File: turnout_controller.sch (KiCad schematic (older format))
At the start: 29 parts, among them J1 DCC_A, J2 DCC_B, J3 PROG, J4 MOT_CNTL, J5 MOT_POWER, J6 MOT_GND, J7 LED_1, J8 LED_2, SW1 SW_Push, SW2 SW_Push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

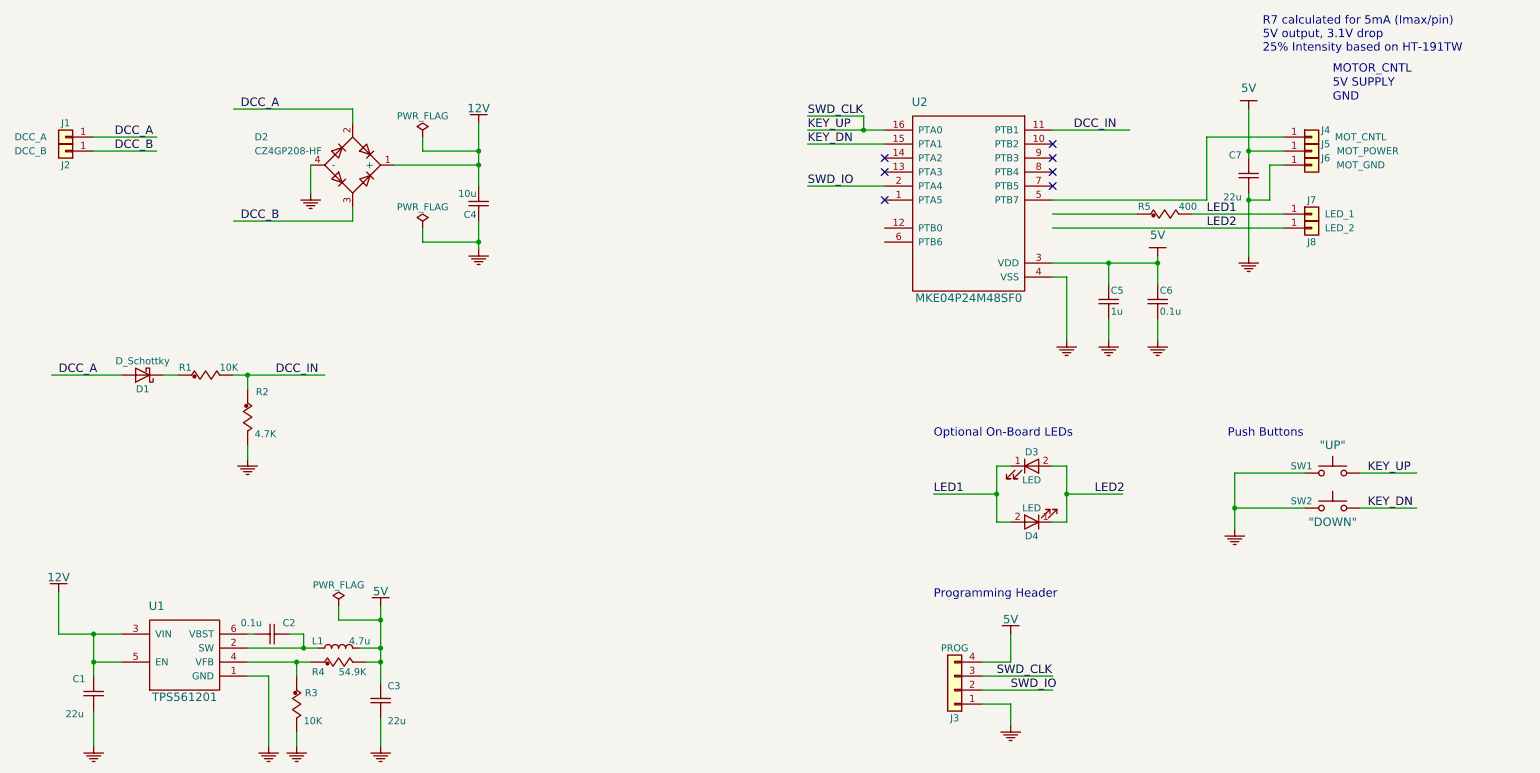
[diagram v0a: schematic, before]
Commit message: Board revision 3.0 - prog header @ top
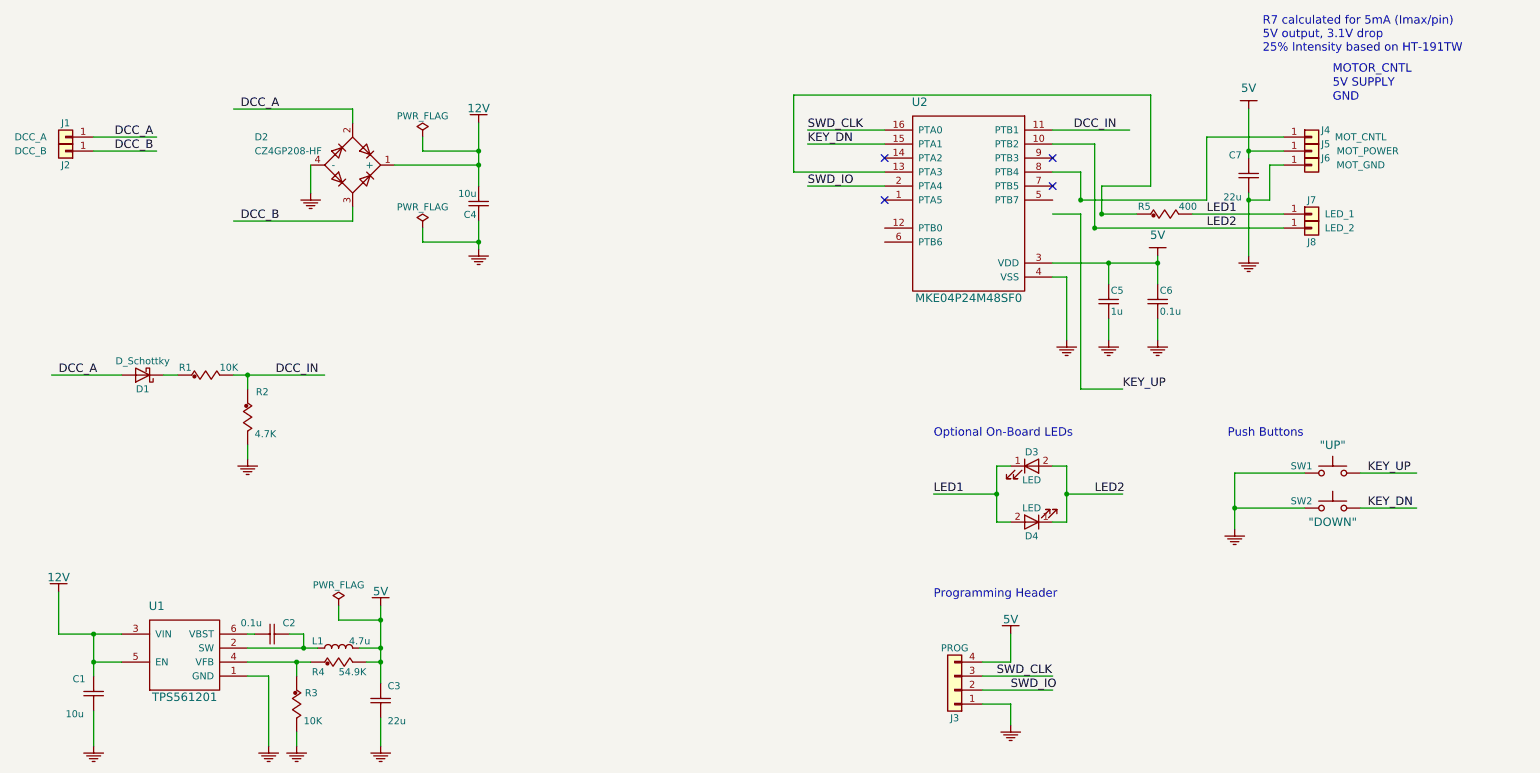
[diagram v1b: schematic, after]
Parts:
- C1: value 22u -> 10u
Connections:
- wire segments 83 -> 94
- no-connect marks 7 -> 4
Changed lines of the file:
@@
 $EndComp
 NoConn ~ 7950 1600
-NoConn ~ 7950 1700
 NoConn ~ 7950 1800
 NoConn ~ 6750 1600
-NoConn ~ 6750 1700
-Text Label 6200 1400 0    60   ~ 0
+Text Label 8450 3250 0    60   ~ 0
 KEY_UP
 Text Label 6200 1500 0    60   ~ 0
@@
 Text Label 2400 3150 0    60   ~ 0
 DCC_IN
-NoConn ~ 7950 1500
 Text Notes 9450 850  0    60   ~ 0
 R7 calculated for 5mA (Imax/pin)\n5V output, 3.1V drop\n25% Intensity based on HT-191TW\n
@@
 	1    0    0    -1
 $EndComp
-Text Label 6200 1300 0    60   ~ 0
+Text Label 6200 1400 0    60   ~ 0
 SWD_CLK
 NoConn ~ 6750 1900
@@
 	0    -1   -1   0
 $EndComp
-Wire Wire Line
-	7950 2450 8050 2450
-Wire Wire Line
-	7950 2350 8700 2350
-Connection ~ 8350 2350
-Wire Wire Line
-	7950 2000 8550 2000
-Wire Wire Line
-	7950 1900 9050 1900
-Wire Wire Line
-	8950 2000 9600 2000
-Wire Wire Line
-	3850 1350 3850 1800
-Connection ~ 3850 1650
-Wire Wire Line
-	3850 2050 3850 2250
-Wire Wire Line
-	8350 2350 8350 2500
-Wire Wire Line
-	8700 2300 8700 2500
-Wire Wire Line
-	2200 3650 2200 3750
-Wire Wire Line
-	2650 1650 2650 1850
-Wire Wire Line
-	2950 1950 2950 2050
-Wire Wire Line
-	2950 2050 2100 2050
-Wire Wire Line
-	1100 1550 1550 1550
-Wire Wire Line
-	1100 1450 1550 1450
-Wire Wire Line
-	2100 1250 2950 1250
-Wire Wire Line
-	7950 1400 8500 1400
-Wire Wire Line
-	1600 3150 1700 3150
-Wire Wire Line
-	2100 3150 2750 3150
-Wire Wire Line
-	2200 3150 2200 3250
-Connection ~ 2200 3150
-Wire Wire Line
-	8050 2450 8050 2900
-Wire Wire Line
-	8350 2750 8350 2900
-Wire Wire Line
-	8700 2750 8700 2900
-Wire Wire Line
-	9350 1850 9350 2300
-Wire Wire Line
-	9500 1650 9600 1650
-Wire Wire Line
-	9050 1900 9050 1450
-Wire Wire Line
-	9050 1450 9600 1450
-Wire Wire Line
-	9350 1900 9500 1900
-Wire Wire Line
-	9500 1900 9500 1650
-Connection ~ 9350 1900
-Wire Wire Line
-	6200 1500 6750 1500
-Wire Wire Line
-	3250 1650 3850 1650
-Connection ~ 8700 2350
-Wire Wire Line
-	6200 1400 6750 1400
-Wire Wire Line
-	10150 4100 10550 4100
-Wire Wire Line
-	10550 3850 10150 3850
-Wire Wire Line
-	9250 3850 9750 3850
-Wire Wire Line
-	9250 3850 9250 4250
-Wire Wire Line
-	9250 4100 9750 4100
-Connection ~ 9250 4100
-Wire Wire Line
-	2950 1250 2950 1350
-Wire Wire Line
-	1300 3150 800  3150
-Wire Wire Line
-	3450 1450 3450 1550
-Wire Wire Line
-	3450 1550 3850 1550
-Connection ~ 3850 1550
-Wire Wire Line
-	3450 2100 3450 2200
-Wire Wire Line
-	3450 2200 3850 2200
-Connection ~ 3850 2200
-Wire Wire Line
-	9350 1250 9350 1600
-Wire Wire Line
-	9600 1550 9350 1550
-Connection ~ 9350 1550
-Wire Wire Line
-	6600 1300 6600 1400
-Wire Wire Line
-	6200 1300 6600 1300
-Connection ~ 6600 1400
-Wire Wire Line
-	6750 1800 6200 1800
-Wire Wire Line
-	7450 5300 7950 5300
-Wire Wire Line
-	7450 5400 7950 5400
-Wire Wire Line
-	7450 5200 7650 5200
-Wire Wire Line
-	7650 5200 7650 5000
-Wire Wire Line
-	7450 5500 7650 5500
-Wire Wire Line
-	7650 5500 7650 5650
-Wire Wire Line
-	7550 4200 7650 4200
-Wire Wire Line
-	7550 3800 7550 4200
-Wire Wire Line
-	7550 3800 7650 3800
-Wire Wire Line
-	8050 4200 7950 4200
-Wire Wire Line
-	8050 3800 8050 4200
-Wire Wire Line
-	8050 3800 7950 3800
-Connection ~ 7550 4000
-Connection ~ 8050 4000
-Wire Wire Line
-	7950 2100 9600 2100
-Wire Wire Line
-	7100 4000 7550 4000
-Wire Wire Line
-	8050 4000 8450 4000
-Wire Wire Line
-	2200 5300 2350 5300
-Wire Wire Line
-	2350 5300 2350 5800
-Wire Wire Line
-	850  5000 1300 5000
-Wire Wire Line
-	850  5000 850  4700
-Wire Wire Line
-	1100 5000 1100 5300
-Connection ~ 1100 5000
 $Comp
 L CAP_NP C1
@@
 P 1100 5550
 F 0 "C1" H 950 5750 50  0000 L BNN
-F 1 "22u" H 900 5500 50  0000 L BNN
+F 1 "10u" H 900 5500 50  0000 L BNN
 F 2 "Capacitors_SMD:C_0603_HandSoldering" H 1175 5450 40  0001 L BNN
 F 3 "" H 1100 5550 60  0000 C CNN
@@
 	1    0    0    -1
 $EndComp
-Wire Wire Line
-	1100 5550 1100 5800
-Wire Wire Line
-	1300 5200 1100 5200
-Connection ~ 1100 5200
-Wire Wire Line
-	2200 5100 2700 5100
-Wire Wire Line
-	2200 5200 2650 5200
-Wire Wire Line
-	2550 5200 2550 5300
-Wire Wire Line
-	2550 5700 2550 5800
-Connection ~ 2550 5200
 $Comp
 L CAP_NP C3
@@
 	1    0    0    -1
 $EndComp
-Wire Wire Line
-	3150 5200 3050 5200
-Wire Wire Line
-	3150 4800 3150 5350
-Wire Wire Line
-	3000 5100 3150 5100
-Connection ~ 3150 5200
-Connection ~ 3150 5100
-Wire Wire Line
-	2850 4800 2850 4900
-Wire Wire Line
-	2850 4900 3150 4900
-Connection ~ 3150 4900
 $Comp
 L GND_ #PWR022
@@
 	1    0    0    -1
 $EndComp
-Wire Wire Line
-	3150 5800 3150 5600
 $Comp
 L CAP_NP C2
@@
 $EndComp
 Wire Wire Line
+	7950 2450 8050 2450
+Wire Wire Line
+	7950 2350 8700 2350
+Connection ~ 8350 2350
+Wire Wire Line
+	8300 2000 8550 2000
+Wire Wire Line
+	8150 1900 9050 1900
+Wire Wire Line
+	8950 2000 9600 2000
+Wire Wire Line
+	3850 1350 3850 1800
+Connection ~ 3850 1650
+Wire Wire Line
+	3850 2050 3850 2250
+Wire Wire Line
+	8350 2350 8350 2500
+Wire Wire Line
+	8700 2300 8700 2500
+Wire Wire Line
+	2200 3650 2200 3750
+Wire Wire Line
+	2650 1650 2650 1850
+Wire Wire Line
+	2950 1950 2950 2050
+Wire Wire Line
+	2950 2050 2100 2050
+Wire Wire Line
+	1100 1550 1550 1550
+Wire Wire Line
+	1100 1450 1550 1450
+Wire Wire Line
+	2100 1250 2950 1250
+Wire Wire Line
+	7950 1400 8500 1400
+Wire Wire Line
+	1600 3150 1700 3150
+Wire Wire Line
+	2100 3150 2750 3150
+Wire Wire Line
+	2200 3150 2200 3250
+Connection ~ 2200 3150
+Wire Wire Line
+	8050 2450 8050 2900
+Wire Wire Line
+	8350 2750 8350 2900
+Wire Wire Line
+	8700 2750 8700 2900
+Wire Wire Line
+	9350 1850 9350 2300
+Wire Wire Line
+	9500 1650 9600 1650
+Wire Wire Line
+	9050 1900 9050 1450
+Wire Wire Line
+	9050 1450 9600 1450
+Wire Wire Line
+	9350 1900 9500 1900
+Wire Wire Line
+	9500 1900 9500 1650
+Connection ~ 9350 1900
+Wire Wire Line
+	6200 1500 6750 1500
+Wire Wire Line
+	3250 1650 3850 1650
+Connection ~ 8700 2350
+Wire Wire Line
+	10150 4100 10550 4100
+Wire Wire Line
+	10550 3850 10150 3850
+Wire Wire Line
+	9250 3850 9750 3850
+Wire Wire Line
+	9250 3850 9250 4250
+Wire Wire Line
+	9250 4100 9750 4100
+Connection ~ 9250 4100
+Wire Wire Line
+	2950 1250 2950 1350
+Wire Wire Line
+	1300 3150 800  3150
+Wire Wire Line
+	3450 1450 3450 1550
+Wire Wire Line
+	3450 1550 3850 1550
+Connection ~ 3850 1550
+Wire Wire Line
+	3450 2100 3450 2200
+Wire Wire Line
+	3450 2200 3850 2200
+Connection ~ 3850 2200
+Wire Wire Line
+	9350 1250 9350 1600
+Wire Wire Line
+	9600 1550 9350 1550
+Connection ~ 9350 1550
+Wire Wire Line
+	6750 1800 6200 1800
+Wire Wire Line
+	7450 5300 7950 5300
+Wire Wire Line
+	7450 5400 7950 5400
+Wire Wire Line
+	7450 5200 7650 5200
+Wire Wire Line
+	7650 5200 7650 5000
+Wire Wire Line
+	7450 5500 7650 5500
+Wire Wire Line
+	7650 5500 7650 5650
+Wire Wire Line
+	7550 4200 7650 4200
+Wire Wire Line
+	7550 3800 7550 4200
+Wire Wire Line
+	7550 3800 7650 3800
+Wire Wire Line
+	8050 4200 7950 4200
+Wire Wire Line
+	8050 3800 8050 4200
+Wire Wire Line
+	8050 3800 7950 3800
+Connection ~ 7550 4000
+Connection ~ 8050 4000
+Wire Wire Line
+	8250 2100 9600 2100
+Wire Wire Line
+	7100 4000 7550 4000
+Wire Wire Line
+	8050 4000 8450 4000
+Wire Wire Line
+	2200 5300 2350 5300
+Wire Wire Line
+	2350 5300 2350 5800
+Wire Wire Line
+	850  5000 1300 5000
+Wire Wire Line
+	850  5000 850  4700
+Wire Wire Line
+	1100 5000 1100 5300
+Connection ~ 1100 5000
+Wire Wire Line
+	1100 5550 1100 5800
+Wire Wire Line
+	1300 5200 1100 5200
+Connection ~ 1100 5200
+Wire Wire Line
+	2200 5100 2700 5100
+Wire Wire Line
+	2200 5200 2650 5200
+Wire Wire Line
+	2550 5200 2550 5300
+Wire Wire Line
+	2550 5700 2550 5800
+Connection ~ 2550 5200
+Wire Wire Line
+	3150 5200 3050 5200
+Wire Wire Line
+	3150 4800 3150 5350
+Wire Wire Line
+	3000 5100 3150 5100
+Connection ~ 3150 5200
+Connection ~ 3150 5100
+Wire Wire Line
+	2850 4800 2850 4900
+Wire Wire Line
+	2850 4900 3150 4900
+Connection ~ 3150 4900
+Wire Wire Line
+	3150 5800 3150 5600
+Wire Wire Line
 	2500 5000 2600 5000
 Wire Wire Line
@@
 Wire Wire Line
 	2250 5000 2200 5000
+Wire Wire Line
+	6750 1700 6100 1700
+Wire Wire Line
+	6100 1700 6100 1150
+Wire Wire Line
+	6100 1150 8650 1150
+Wire Wire Line
+	8650 1150 8650 1800
+Wire Wire Line
+	8650 1800 8300 1800
+Wire Wire Line
+	8300 1800 8300 2000
+Connection ~ 8300 2000
+Wire Wire Line
+	7950 1700 8150 1700
+Wire Wire Line
+	8150 1700 8150 1900
+Connection ~ 8150 1900
+Wire Wire Line
+	7950 1500 8250 1500
+Wire Wire Line
+	8250 1500 8250 2100
+Connection ~ 8250 2100
+Wire Wire Line
+	6200 1400 6750 1400
+Wire Wire Line
+	7950 2000 8150 2000
+Wire Wire Line
+	8150 2000 8150 3250
+Wire Wire Line
+	8150 3250 8450 3250
 $EndSCHEMATC
